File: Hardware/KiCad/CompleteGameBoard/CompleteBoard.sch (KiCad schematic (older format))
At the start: 21 parts

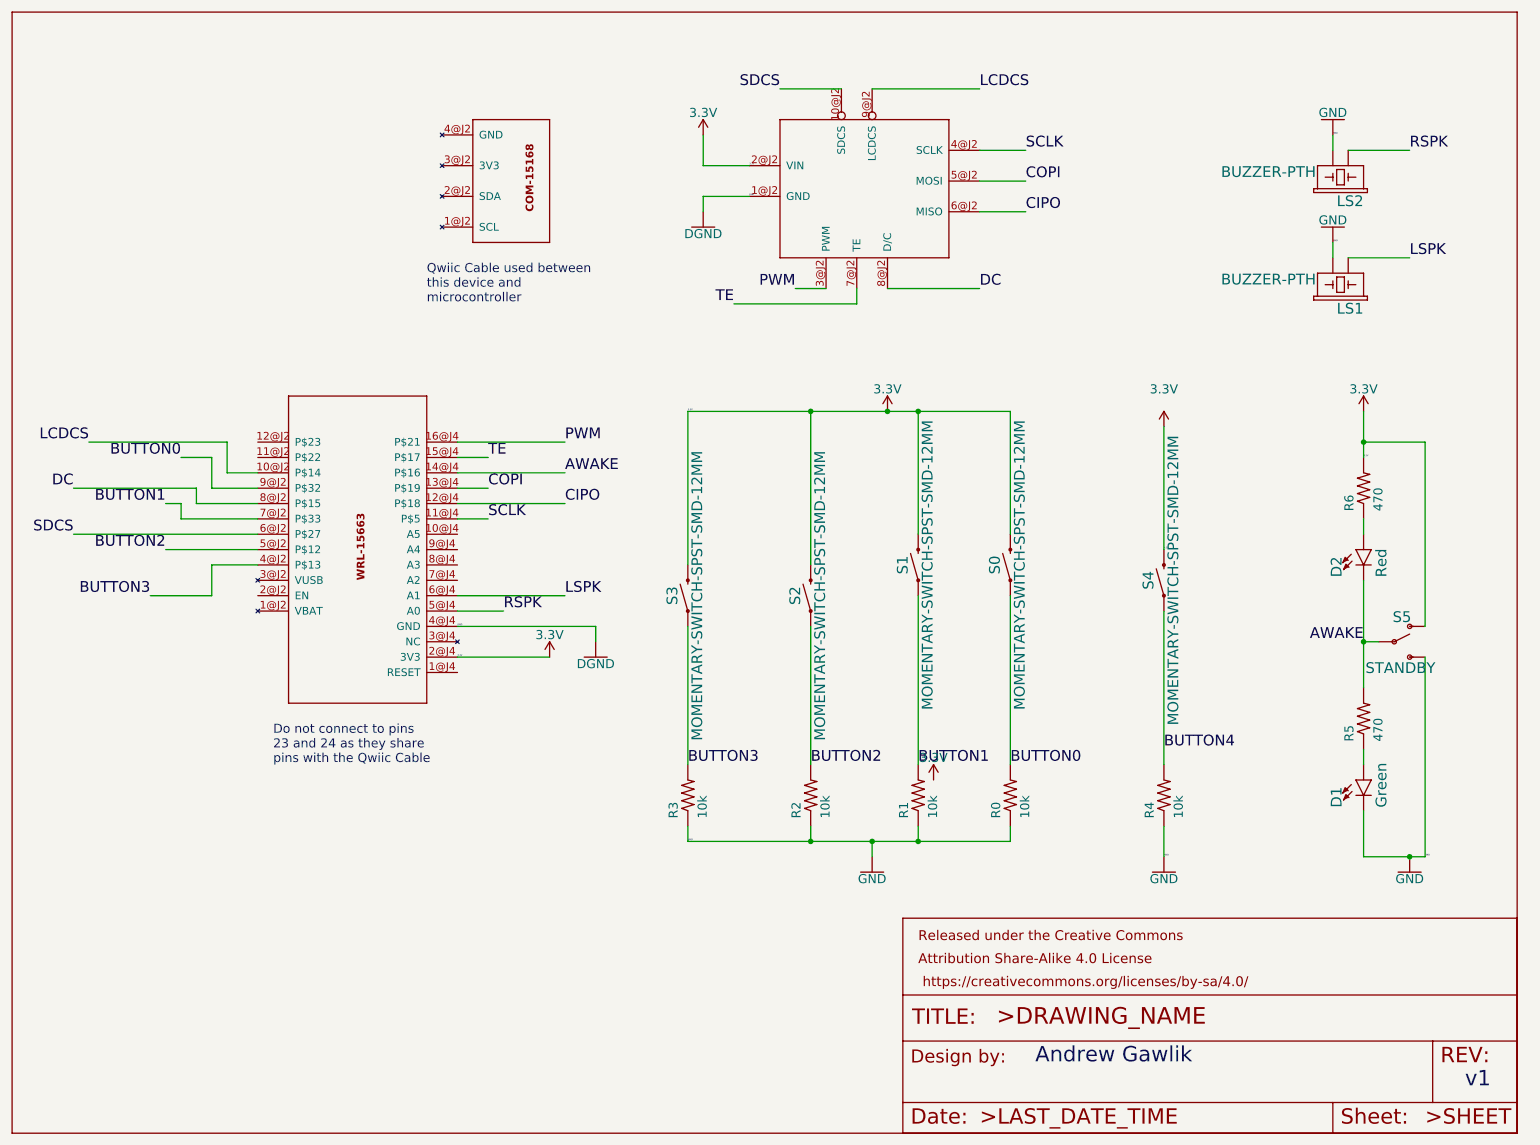
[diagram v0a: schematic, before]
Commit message: Re-imported updated EagleCAD board for issue #12
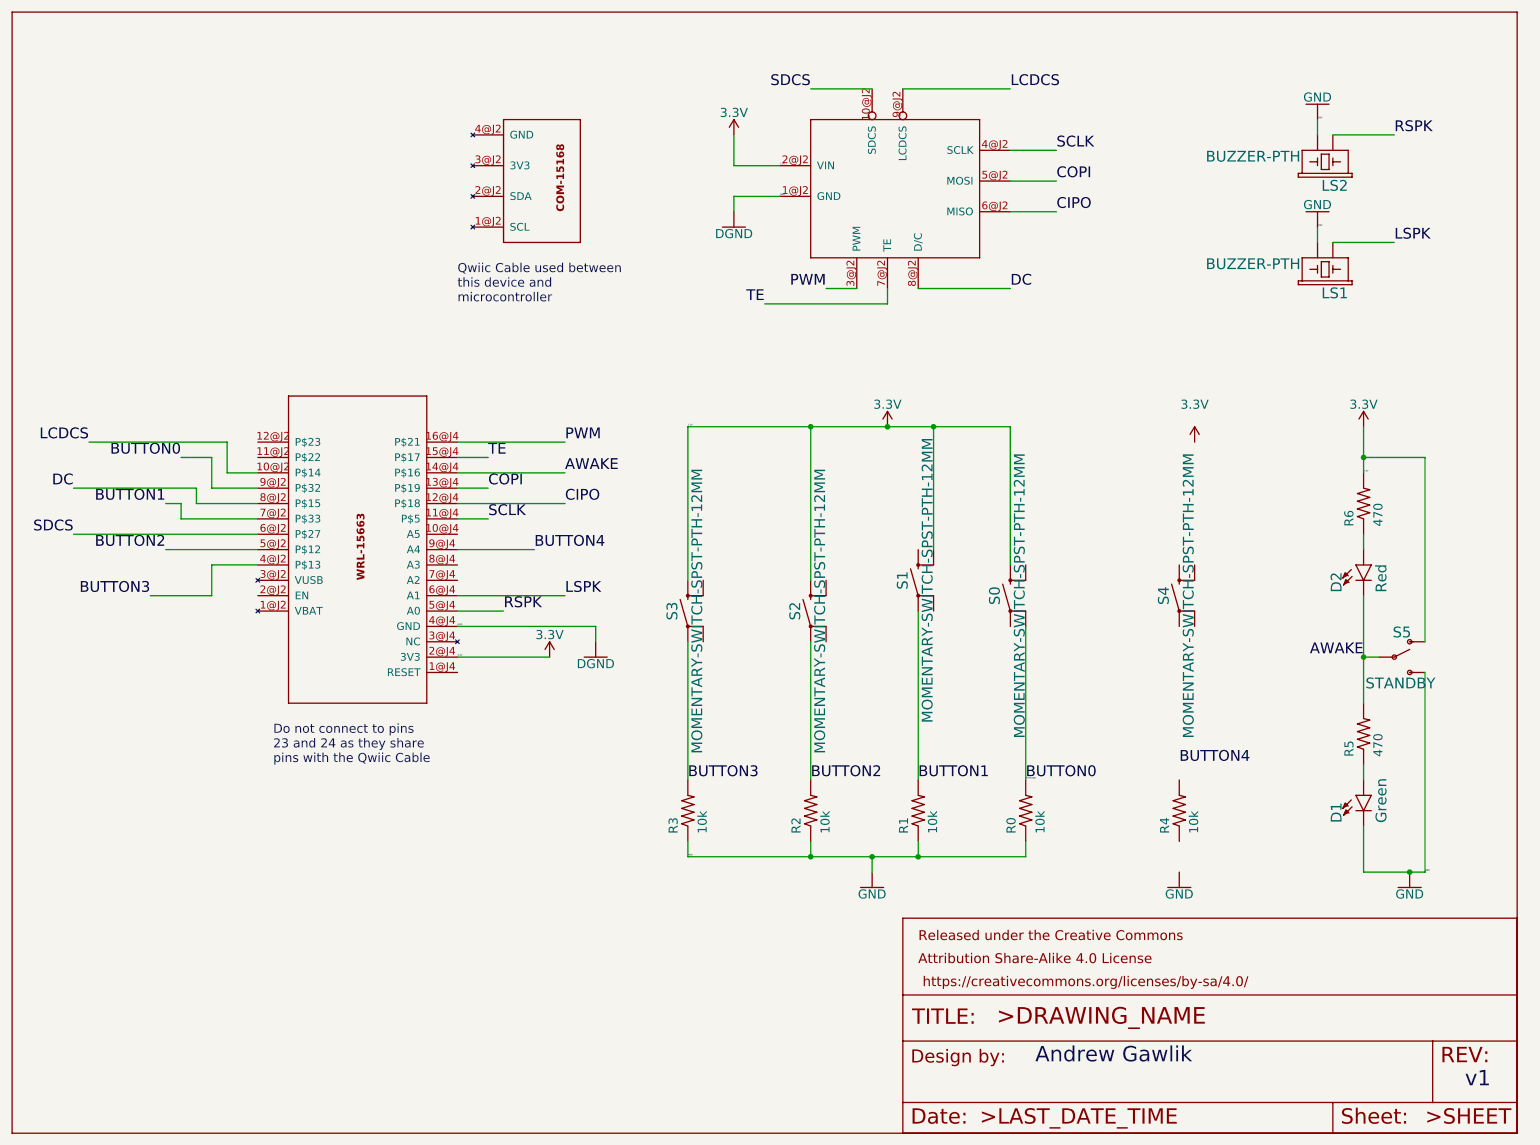
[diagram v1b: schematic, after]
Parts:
- removed S0, S1, S2, S3, S4: MOMENTARY-SWITCH-SPST-SMD-12MM, CompleteBoard:TACTILE_SWITCH_SMD_12MM, symbol CompleteBoard-eagle-import:MOMENTARY-SWITCH-SPST-SMD-12MM
- added S0, S1, S2, S3, S4: MOMENTARY-SWITCH-SPST-PTH-12MM, CompleteBoard:TACTILE_SWITCH_PTH_12MM, symbol CompleteBoard-eagle-import:MOMENTARY-SWITCH-SPST-PTH-12MM
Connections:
- net 3.3V: now also S0.3, S1.4, S2.3, S3.3
- net BUTTON0: now also S0.2
- net BUTTON1: now also S1.1
- net BUTTON2: now also S2.1
- net BUTTON3: now also S3.1
- net BUTTON4: now also A1.9@J4 (A4); no longer R4.2
- net GND: no longer R4.1
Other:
- moved on the sheet: D1, D2, LS1, LS2, R0, R1, R2, R3, R4, R5, R6, S5
